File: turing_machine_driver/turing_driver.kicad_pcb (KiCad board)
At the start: 2 copper layers, 165.1 x 110.5 mm, 107 parts, among them J1 Buttons and Switches connector, J2 Header Position Value, J3 Symbol Register Value, J4 State Register Value, J5 External Interface, Q1 55NF06, U1 74LS14, U10 74LS245, U11 SST39SF020, U12 74LS245, U13 74LS245, U14 74LS245, U15 D5631LA, U16 D5631LR, U17 74LS245, U2 74LS03, U3 74LS04, U4 74LS139, U5 74LS74, U6 NE555P, U7 NE555P, U8 NE555P, U9 74LS245

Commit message: added control panel and moved LEDs to it
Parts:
- removed the D1 at (-199.0, 40.3)
- removed D10: LED_HEADER2, LED_THT:LED_D5.0mm
- removed D11: LED_HEADER3, LED_THT:LED_D5.0mm
- removed D12: LED_HEADER4, LED_THT:LED_D5.0mm
- removed D13: LED_HEADER5, LED_THT:LED_D5.0mm
- removed D14: LED_HEADER6, LED_THT:LED_D5.0mm
- removed D15: LED_HEADER7, LED_THT:LED_D5.0mm
- removed D16: LED_HEADER8, LED_THT:LED_D5.0mm
- removed D17: LED_HEADER9, LED_THT:LED_D5.0mm
- removed D18: LED_HEADER10, LED_THT:LED_D5.0mm
- removed D19: LED_HEADER11, LED_THT:LED_D5.0mm
- removed D2: LED_PROGRAM_R, LED_THT:LED_D5.0mm
- removed D20: LED_HEADER12, LED_THT:LED_D5.0mm
- removed D21: LED_HEADER13, LED_THT:LED_D5.0mm
- removed D22: LED_HEADER14, LED_THT:LED_D5.0mm
- removed D23: LED_HEADER15, LED_THT:LED_D5.0mm
- removed D3: LED_RESET_Y, LED_THT:LED_D5.0mm
- removed D4: LED_FINISH_STATE_Y, LED_THT:LED_D5.0mm
- removed D5: LED_SESR_STATE_G, LED_THT:LED_D5.0mm
- removed D6: LED_CLK_G, LED_THT:LED_D5.0mm
- removed D8: LED_HEADER0, LED_THT:LED_D5.0mm
- removed D9: LED_HEADER1, LED_THT:LED_D5.0mm
- removed the R15 at (-151.6, 65.3)
- removed R16, R17, R18, R19, R20, R22, R23, R24, R25, R26, R27, R28, R29, R30, R31, R32, R33, R34, R35, R36, R37: 330Ω, Resistor_THT:R_Axial_DIN0207_L6.3mm_D2.5mm_P10.16mm_Horizontal
- removed the U15 at (-150.4, 39.9)
- removed U16: D5631LR, Display_7Segment:DA56-11CGKWA
- added J6: Signal_connector_1, Connector_Edge:Connector_Edge_2x17pin_odd, F.Cu at (20.3, 129.5)
- added J7: Signal_connector_0, Connector_Edge:Connector_Edge_2x17pin_odd, F.Cu at (20.3, 73.7)
- added REF**: MountingHole_3.2mm_M3, MountingHole:MountingHole_3.2mm_M3, F.Cu at (186.7, 29.2)
- added REF**: MountingHole_3.2mm_M3, MountingHole:MountingHole_3.2mm_M3, F.Cu at (186.7, 132.1)
- added REF**: MountingHole_3.2mm_M3, MountingHole:MountingHole_3.2mm_M3, F.Cu at (29.2, 132.1)
- added REF**: MountingHole_3.2mm_M3, MountingHole:MountingHole_3.2mm_M3, F.Cu at (29.2, 29.2)
- J1: value Buttons and Switches connector -> RPi Interface; footprint Connector_IDC:IDC-Header_2x07_P2.54mm_Horizontal -> Connector_IDC:IDC-Header_2x10_P2.54mm_Vertical
- RN1: value 1,5kΩ -> R_Pack04_SIP; footprint Connector_PinSocket_2.54mm:PinSocket_1x08_P2.54mm_Vertical -> Resistor_THT:R_Array_SIP8
- RN2: value 680Ω -> R_Pack04_SIP; footprint Connector_PinSocket_2.54mm:PinSocket_1x08_P2.54mm_Vertical -> Resistor_THT:R_Array_SIP8
- moved U9 337.7 mm to (124.5, 105.4)
- moved U10 310.3 mm to (106.7, 105.4)
- moved A1 268.5 mm to (161.9, 29.4)
- moved J1 263.8 mm to (176.5, 84.5), turned to -90 degrees
- moved U3 260.7 mm to (177.8, 113.0)
- moved D1 256.5 mm to (64.8, 30.5)
- moved U12 251.5 mm to (71.1, 43.2)
- moved U11 243.0 mm to (55.9, 128.3), turned to 90 degrees
- moved U4 229.4 mm to (160.0, 110.5)
- moved U13 223.7 mm to (35.6, 105.4)
- moved R15 220.7 mm to (61.0, 30.5), turned to 180 degrees
- moved U5 218.8 mm to (142.2, 113.0)
- moved U14 212.5 mm to (53.3, 43.2)
- moved RN1 209.6 mm to (50.5, 110.5), turned to -90 degrees
- moved RN2 201.9 mm to (46.4, 110.5), turned to -90 degrees
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- renumbered C19 to C18, C18 to C19, D7 to D1, R9 to R10, R10 to R12, R21 to R15, R8 to R5, R5 to R6, R6 to R7, R7 to R8, R12 to R9, U17 to U15
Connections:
- A1 pad 13: LPS_{2} -> RRB_{1}
- A1 pad 18: LPS_{2} -> RRB_{1}
- A1 pad 23: LPS_{2} -> RRB_{1}
- A1 pad 28: LPS_{2} -> RRB_{1}
- A1 pad 3: LPS_{2} -> RRB_{1}
- A1 pad 38: LPS_{2} -> RRB_{1}
- A1 pad 8: LPS_{2} -> RRB_{1}
- C1 pad 2: LPS_{2} -> RRB_{1}
- C10 pad 2: LPS_{2} -> RRB_{1}
- C11 pad 2: LPS_{2} -> RRB_{1}
- C12 pad 2: LPS_{2} -> RRB_{1}
- C13 pad 2: LPS_{2} -> RRB_{1}
- C14 pad 2: LPS_{2} -> RRB_{1}
- C15 pad 2: LPS_{2} -> RRB_{1}
- C16 pad 2: LPS_{2} -> RRB_{1}
- C17 pad 2: LPS_{2} -> RRB_{1}
- C18 pad 2: LPS_{2} -> RRB_{1}
- C19 pad 2: LPS_{2} -> RRB_{1}
- C2 pad 2: LPS_{2} -> RRB_{1}
- C20 pad 2: LPS_{2} -> RRB_{1}
- C21 pad 2: LPS_{2} -> RRB_{1}
- C3 pad 2: LPS_{2} -> RRB_{1}
- C4 pad 2: LPS_{2} -> RRB_{1}
- C5 pad 2: LPS_{2} -> RRB_{1}
- C6 pad 2: LPS_{2} -> RRB_{1}
- C7 pad 2: LPS_{2} -> RRB_{1}
- C8 pad 2: LPS_{2} -> RRB_{1}
- C9 pad 2: LPS_{2} -> RRB_{1}
- J1 pad 1: MCB_{0} -> RRB_{1}
- J1 pad 10: LPS_{1} -> ~{DT}
- J1 pad 11: LPS_{2} -> CS_{0}
- J1 pad 12: LBP_{0} -> CS_{1}
- J1 pad 13: LBP_{1} -> D_{6}
- J1 pad 14: LBP_{2} -> D_{7}
- J1 pad 2: MCB_{1} -> LPS_{0}
- J1 pad 3: COM_{0} -> COMBINED_CLK
- J1 pad 4: COM_{1} -> /REPROGRAM
- J1 pad 5: ACP_{0} -> ~{PROGRAM}
- J1 pad 6: ACP_{1} -> ~{FINISH_STATE}
- J1 pad 7: RRB_{0} -> RPI_CLK
- J1 pad 8: LPS_{2} -> ~{RESET}
- J1 pad 9: LPS_{0} -> DDIR
- J5 pad 18: LPS_{2} -> RRB_{1}
- J5 pad 20: LPS_{2} -> RRB_{1}
- J5 pad 22: LPS_{2} -> RRB_{1}
- J5 pad 24: LPS_{2} -> RRB_{1}
- J5 pad 26: LPS_{2} -> RRB_{1}
- J5 pad 28: LPS_{2} -> RRB_{1}
- Q1 pad 3: LPS_{2} -> RRB_{1}
- RN1 pad 2: Net-(RN1-R2.1) -> 7SEG_A
- RN1 pad 3: Net-(RN1-R3.1) -> Net-(RN1-R2.1)
- RN1 pad 4: Net-(RN1-R4.1) -> 7SEG_B
- RN1 pad 5: /LED display/7SEG_D -> Net-(RN1-R3.1)
- RN1 pad 6: /LED display/7SEG_C -> 7SEG_C
- RN1 pad 7: /LED display/7SEG_B -> Net-(RN1-R4.1)
- RN1 pad 8: /LED display/7SEG_A -> 7SEG_D
- RN2 pad 2: Net-(RN2-R2.1) -> 7SEG_E
- RN2 pad 3: Net-(RN2-R3.1) -> Net-(RN2-R2.1)
- RN2 pad 4: Net-(RN2-R4.1) -> 7SEG_F
- RN2 pad 5: /LED display/7SEG_DP -> Net-(RN2-R3.1)
- RN2 pad 6: /LED display/7SEG_G -> 7SEG_G
- RN2 pad 7: /LED display/7SEG_F -> unconnected-(RN2-R4.1-Pad7)
- RN2 pad 8: /LED display/7SEG_E -> unconnected-(RN2-R4.2-Pad8)
- U1 pad 7: LPS_{2} -> RRB_{1}
- U10 pad 10: LPS_{2} -> RRB_{1}
- U10 pad 11: unconnected-(U10-B7-Pad11) -> Net-(U10-B7)
- U10 pad 18: Net-(U10-B0) -> unconnected-(U10-B0-Pad18)
- U10 pad 19: LPS_{2} -> RRB_{1}
- U10 pad 2: SR_{0} -> RRB_{1}
- U10 pad 3: SR_{1} -> SR_{6}
- U10 pad 4: SR_{2} -> SR_{5}
- U10 pad 5: SR_{3} -> SR_{4}
- U10 pad 6: SR_{4} -> SR_{3}
- U10 pad 7: SR_{5} -> SR_{2}
- U10 pad 8: SR_{6} -> SR_{1}
- U10 pad 9: LPS_{2} -> SR_{0}
- U11 pad 1: LPS_{2} -> RRB_{1}
- U11 pad 10: Net-(U11-A2) -> /LED display/QRB_{2}
- U11 pad 11: Net-(U11-A1) -> /LED display/QRB_{1}
- U11 pad 12: Net-(U11-A0) -> /LED display/QRB_{0}
- U11 pad 16: LPS_{2} -> RRB_{1}
- U11 pad 22: LPS_{2} -> RRB_{1}
- U11 pad 23: Net-(U10-B2) -> Net-(U10-B5)
- U11 pad 24: LPS_{2} -> RRB_{1}
- U11 pad 25: Net-(U10-B3) -> Net-(U10-B4)
- U11 pad 26: Net-(U10-B1) -> Net-(U10-B6)
- U11 pad 27: Net-(U10-B0) -> Net-(U10-B7)
- U11 pad 28: Net-(U10-B5) -> Net-(U10-B2)
- U11 pad 29: Net-(U10-B6) -> Net-(U10-B1)
- U11 pad 30: LPS_{2} -> RRB_{1}
- U11 pad 4: Net-(U10-B4) -> Net-(U10-B3)
- U11 pad 5: Net-(U11-A7) -> /LED display/QRB_{7}
- U11 pad 6: Net-(U11-A6) -> /LED display/QRB_{6}
- U11 pad 7: Net-(U11-A5) -> /LED display/QRB_{5}
- U11 pad 8: Net-(U11-A4) -> /LED display/QRB_{4}
- U11 pad 9: Net-(U11-A3) -> /LED display/QRB_{3}
- U12 pad 10: LPS_{2} -> RRB_{1}
- U12 pad 13: Net-(D6-A) -> CLK
- U12 pad 14: Net-(D5-A) -> LED_SESR_STATE
- U12 pad 15: Net-(D4-A) -> LED_FINISH_STATE
- U12 pad 16: Net-(D3-A) -> LED_RESET
- U12 pad 17: Net-(D2-A) -> LED_OPERATE
- U12 pad 18: Net-(D1-A) -> LED_PROGRAM
- U12 pad 8: LPS_{2} -> RRB_{1}
- U12 pad 9: LPS_{2} -> RRB_{1}
- U13 pad 10: LPS_{2} -> RRB_{1}
- U13 pad 11: Net-(RN2-R4.1) -> unconnected-(U13-B7-Pad11)
- U14 pad 1: LPS_{0} -> RRB_{1}
- U14 pad 10: LPS_{2} -> RRB_{1}
- U14 pad 11: Net-(D15-A) -> H_{0}
- U14 pad 12: Net-(D14-A) -> H_{1}
- U14 pad 13: Net-(D13-A) -> H_{2}
- U14 pad 14: Net-(D12-A) -> H_{3}
- U14 pad 15: Net-(D11-A) -> H_{4}
- U14 pad 16: Net-(D10-A) -> H_{5}
- U14 pad 17: Net-(D9-A) -> H_{6}
- U14 pad 18: Net-(D8-A) -> H_{7}
- U14 pad 2: H_{0} -> LED_H_{7}
- U14 pad 3: H_{1} -> LED_H_{6}
- U14 pad 4: H_{2} -> LED_H_{5}
- U14 pad 5: H_{3} -> LED_H_{4}
- U14 pad 6: H_{4} -> LED_H_{3}
- U14 pad 7: H_{5} -> LED_H_{2}
- U14 pad 8: H_{6} -> LED_H_{1}
- U14 pad 9: H_{7} -> LED_H_{0}
- U15 pad 1: LPS_{0} -> RRB_{1}
- U15 pad 10: LPS_{2} -> RRB_{1}
- U15 pad 11: Net-(D23-A) -> H_{8}
- U15 pad 12: Net-(D22-A) -> H_{9}
- U15 pad 13: Net-(D21-A) -> H_{10}
- U15 pad 14: Net-(D20-A) -> H_{11}
- U15 pad 15: Net-(D19-A) -> H_{12}
- U15 pad 16: Net-(D18-A) -> H_{13}
- U15 pad 17: Net-(D17-A) -> H_{14}
- U15 pad 18: Net-(D16-A) -> H_{15}
- U15 pad 2: H_{8} -> LED_H_{15}
- U15 pad 3: H_{9} -> LED_H_{14}
- U15 pad 4: H_{10} -> LED_H_{13}
- U15 pad 5: H_{11} -> LED_H_{12}
- U15 pad 6: H_{12} -> LED_H_{11}
- U15 pad 7: H_{13} -> LED_H_{10}
- U15 pad 8: H_{14} -> LED_H_{9}
- U15 pad 9: H_{15} -> LED_H_{8}
- U2 pad 7: LPS_{2} -> RRB_{1}
- U3 pad 2: Net-(U15-DIG2_CA) -> 7SEG_SYMBOL_0
- U3 pad 4: Net-(U15-DIG1_CA) -> 7SEG_SYMBOL_1
- U3 pad 6: Net-(U16-DIG1_CA) -> 7SEG_STATE_0
- U3 pad 7: LPS_{2} -> RRB_{1}
- U3 pad 8: Net-(U16-DIG2_CA) -> 7SEG_STATE_1
- U4 pad 8: LPS_{2} -> RRB_{1}
- U5 pad 7: LPS_{2} -> RRB_{1}
- U6 pad 1: LPS_{2} -> RRB_{1}
- U7 pad 1: LPS_{2} -> RRB_{1}
- U8 pad 1: LPS_{2} -> RRB_{1}
- U9 pad 10: LPS_{2} -> RRB_{1}
- U9 pad 11: Net-(U11-A7) -> /LED display/QRB_{0}
- U9 pad 12: Net-(U11-A6) -> /LED display/QRB_{1}
- U9 pad 13: Net-(U11-A5) -> /LED display/QRB_{2}
- U9 pad 14: Net-(U11-A4) -> /LED display/QRB_{3}
- U9 pad 15: Net-(U11-A3) -> /LED display/QRB_{4}
- U9 pad 16: Net-(U11-A2) -> /LED display/QRB_{5}
- U9 pad 17: Net-(U11-A1) -> /LED display/QRB_{6}
- U9 pad 18: Net-(U11-A0) -> /LED display/QRB_{7}
- U9 pad 19: LPS_{2} -> RRB_{1}
- U9 pad 2: QR_{0} -> QR_{7}
- U9 pad 3: QR_{1} -> QR_{6}
- U9 pad 4: QR_{2} -> QR_{5}
- U9 pad 5: QR_{3} -> QR_{4}
- U9 pad 6: QR_{4} -> QR_{3}
- U9 pad 7: QR_{5} -> QR_{2}
- U9 pad 8: QR_{6} -> QR_{1}
- U9 pad 9: QR_{7} -> QR_{0}
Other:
- outline, holes or cut-outs redrawn
- board text added: "POWER"
- board text added: "STATE"
- board text added: "SYMBOL"
- board text added: "Signal connector 1"
- board text added: "Signal connector 2"

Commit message: finished driver PCB layout
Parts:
- added C10: 100nF, Capacitor_THT:C_Disc_D3.8mm_W2.6mm_P2.50mm, F.Cu at (116.8, 105.4)
- added C12: 100nF, Capacitor_THT:C_Disc_D3.8mm_W2.6mm_P2.50mm, F.Cu at (78.8, 40.0)
- added C14: 100nF, Capacitor_THT:C_Disc_D3.8mm_W2.6mm_P2.50mm, F.Cu at (61.0, 40.0)
- U6, U7, U8: value NE555P -> 555
- moved C3 275.4 mm to (188.0, 110.5), turned to -90 degrees
- moved R14 258.0 mm to (154.3, 66.0), turned to -90 degrees
- moved C4 257.2 mm to (170.2, 110.5), turned to -90 degrees
- moved R7 255.6 mm to (154.3, 45.1), turned to -90 degrees
- moved R13 252.0 mm to (151.1, 76.2), turned to 90 degrees
- moved R6 250.2 mm to (151.1, 55.2), turned to 90 degrees
- moved C5 239.4 mm to (152.4, 113.0), turned to -90 degrees
- moved R9 232.5 mm to (130.2, 66.7), turned to 180 degrees
- moved R10 232.0 mm to (130.2, 57.1), turned to 180 degrees
- moved C7 229.7 mm to (150.5, 42.5)
- moved C8 228.9 mm to (150.5, 63.5)
- moved C19 224.2 mm to (148.0, 55.2), turned to 180 degrees
- moved R11 222.4 mm to (120.0, 63.5)
- moved R12 222.2 mm to (120.0, 60.3)
- moved C24 222.2 mm to (148.0, 76.2), turned to 180 degrees
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- renumbered C10 to C11, C11 to C13, C12 to C15, C13 to C16, C14 to C17, C15 to C18, C16 to C19, C17 to C20, C18 to C21, C19 to C22, C20 to C23, C21 to C24
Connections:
- C17 pad 1: Net-(C14-Pad1) -> (no net)
- C21 pad 1: Net-(C18-Pad1) -> (no net)
- C22 pad 1: Net-(C19-Pad1) -> (no net)
- R1 pad 1: Net-(C14-Pad1) -> Net-(C17-Pad1)
- R10 pad 2: Net-(C19-Pad1) -> Net-(C22-Pad1)
- R11 pad 1: Net-(C18-Pad1) -> Net-(C21-Pad1)
- R12 pad 1: Net-(C19-Pad1) -> Net-(C22-Pad1)
- R2 pad 2: Net-(C14-Pad1) -> Net-(C17-Pad1)
- R9 pad 2: Net-(C18-Pad1) -> Net-(C21-Pad1)
- U1 pad 1: Net-(C19-Pad1) -> Net-(C22-Pad1)
- U1 pad 3: Net-(C18-Pad1) -> Net-(C21-Pad1)
- U1 pad 5: Net-(C14-Pad1) -> Net-(C17-Pad1)
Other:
- board text added: "HEADER"

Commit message: added some wiring and fixed few schematic bugs
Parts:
- U6, U7, U8: value 555 -> NE555P
- moved C11 5.08 mm to (61.0, 110.5)
- moved U11 5.08 mm to (61.0, 128.3)
- moved RN1 3.45 mm to (54.0, 110.5)
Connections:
- C17 pad 1: (no net) -> Net-(C17-Pad1)
- C21 pad 1: (no net) -> Net-(C21-Pad1)
- C22 pad 1: (no net) -> Net-(C22-Pad1)
- R15 pad 2: LED_GND -> RRB_{1}
- U4 pad 13: unconnected-(U4B-A1-Pad13) -> LPS_{0}
- U4 pad 14: unconnected-(U4B-A0-Pad14) -> LPS_{0}
- U4 pad 15: unconnected-(U4B-E-Pad15) -> LPS_{0}
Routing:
- net RRB_{1}: track 0.00 -> 949.8 mm, vias 0 -> 23
- net LPS_{0}: track 0.00 -> 699.9 mm, vias 0 -> 13
- net LPS_{1}: track 0.00 -> 255.4 mm, vias 0 -> 4
- net CLK: track 0.00 -> 201.2 mm, vias 0 -> 6
- net ~{PROGRAM}: track 0.00 -> 177.1 mm, vias 0 -> 5
- net Net-(U11-A16): track 0.00 -> 173.6 mm, vias 0 -> 7
- net SESR_STATE: track 0.00 -> 169.3 mm, vias 0 -> 3
- net Net-(U11-A15): track 0.00 -> 164.6 mm, vias 0 -> 7
- net COMBINED_CLK: track 0.00 -> 158.7 mm, vias 0 -> 7
- net /REPROGRAM: track 0.00 -> 148.4 mm, vias 0 -> 6
- net D_{0}: track 0.00 -> 124.5 mm, vias 0 -> 3
- net D_{1}: track 0.00 -> 124.1 mm, vias 0 -> 4
- net RPI_CLK: track 0.00 -> 118.5 mm, vias 0 -> 3
- net /LED display/QRB_{7}: track 0.00 -> 109.0 mm, vias 0 -> 5
- net D_{2}: track 0.00 -> 108.5 mm, vias 0 -> 3
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
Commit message: finished driver PCB wiring and added some marks
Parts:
- added REF**: KiCad-Logo2_8mm_SilkScreen, Symbol:KiCad-Logo2_8mm_SilkScreen, B.Cu at (93.3, 88.9)
- added REF**: OSHW-Logo_11.4x12mm_SilkScreen, Symbol:OSHW-Logo_11.4x12mm_SilkScreen, B.Cu at (120.7, 90.8)
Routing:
- net 7SEG_STATE_1: track 0.00 -> 207.7 mm, vias 0 -> 5
- net 7SEG_STATE_0: track 0.00 -> 199.3 mm, vias 0 -> 7
- net 7SEG_SYMBOL_1: track 0.00 -> 194.6 mm, vias 0 -> 6
- net 7SEG_SYMBOL_0: track 0.00 -> 191.2 mm, vias 0 -> 7
- net ACP_{0}: track 0.00 -> 179.8 mm, vias 0 -> 4
- net /LED display/RESET: track 0.00 -> 173.6 mm, vias 0 -> 5
- net /LED display/FINISH_STATE: track 0.00 -> 166.4 mm, vias 0 -> 5
- net MCB_{0}: track 0.00 -> 164.1 mm, vias 0 -> 3
- net ACP_{1}: track 21.0 -> 183.2 mm, vias 0 -> 4
- net RRB_{0}: track 0.00 -> 157.2 mm, vias 0 -> 3
- net COM_{0}: track 0.00 -> 153.1 mm, vias 0 -> 3
- net LBP_{1}: track 0.00 -> 144.3 mm, vias 0 -> 3
- net LBP_{2}: track 0.00 -> 126.0 mm, vias 0 -> 3
- net ~{LED_PWR_CLK}: track 40.5 -> 166.4 mm, vias 2 -> 4
- net /Clock and Interfaces/AUTO_CLK: track 0.00 -> 59.0 mm, vias 0 -> 1
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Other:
- outline, holes or cut-outs redrawn
- board text added: "Paweł Szymański 02.2026"
- board text added: "Sterownik Urządzenia"
- board text added: "Tura"

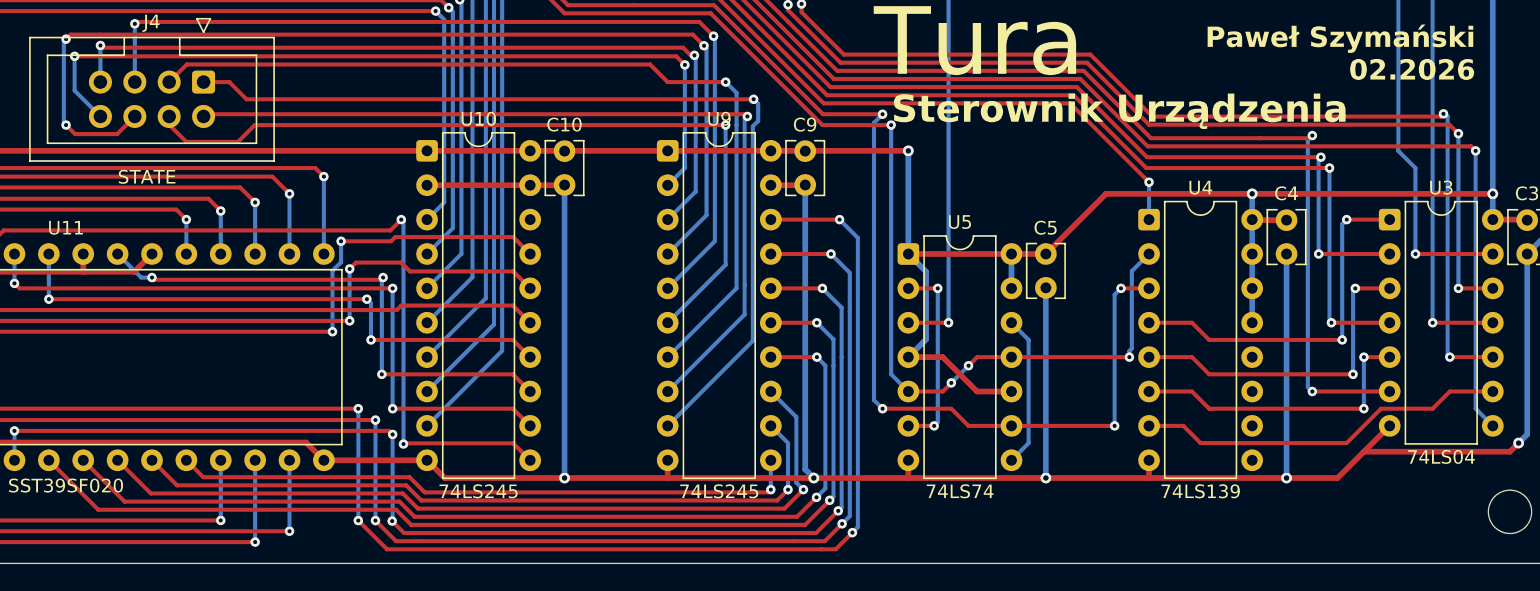
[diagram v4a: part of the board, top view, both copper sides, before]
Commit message: added few markings to PCBs
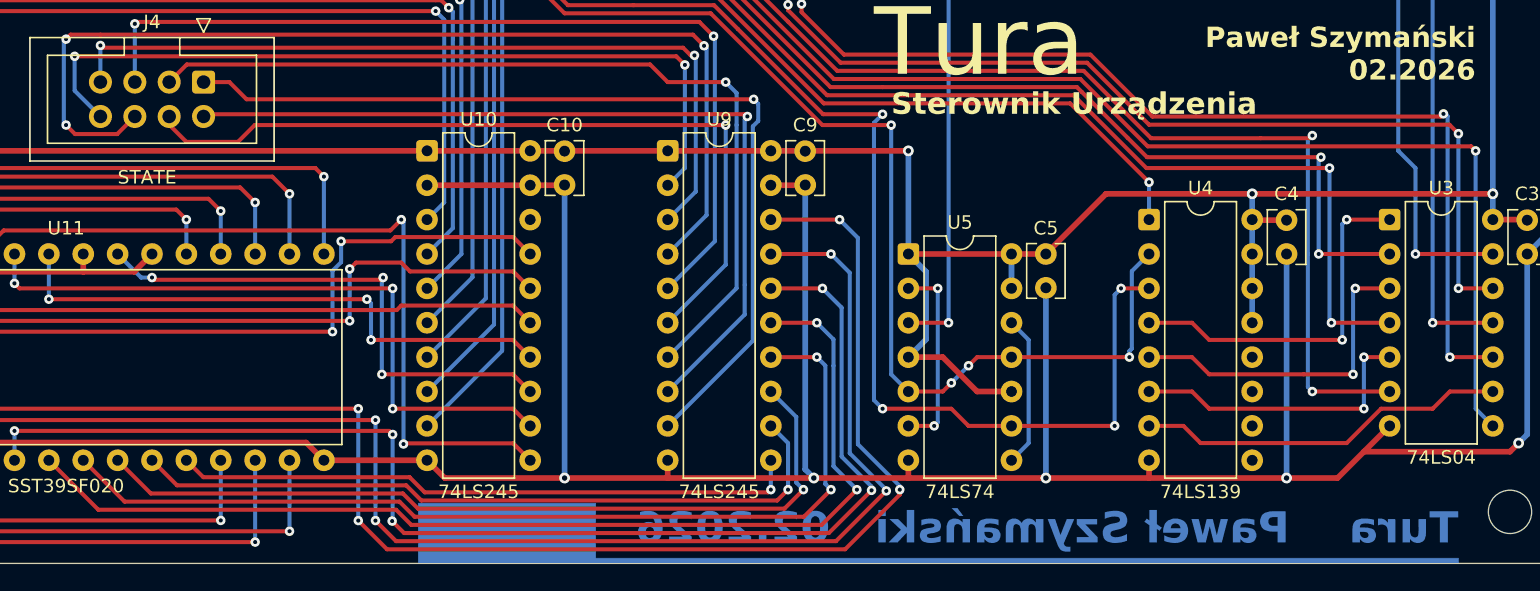
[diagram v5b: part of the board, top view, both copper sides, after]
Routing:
- net /LED display/QRB_{7}: track 109.0 -> 112.0 mm
- net /LED display/QRB_{6}: track 100.2 -> 102.9 mm
- net /LED display/QRB_{5}: track 91.6 -> 94.0 mm
- net /LED display/QRB_{4}: track 77.6 -> 79.7 mm
- net /LED display/QRB_{3}: track 70.8 -> 71.4 mm
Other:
- board text added: "Tura Paweł Szymański 02.2026"
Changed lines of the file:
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@@
 		(net 159)
 	)
+	(gr_rect
+		(start 106.045 131.445)
+		(end 119.126 135.89)
+		(stroke
+			(width 0.05)
+			(type solid)
+		)
+		(fill yes)
+		(layer "B.Cu")
+	)
+	(gr_rect
+		(start 119.126 135.509)
+		(end 182.88 135.89)
+		(stroke
+			(width 0.05)
+			(type solid)
+		)
+		(fill yes)
+		(layer "B.Cu")
+	)
 	(gr_poly
 		(pts
@@
 		(layer "Edge.Cuts")
 	)
+	(gr_text "Tura    Paweł Szymański   02.2026"
+		(at 182.88 134.62 0)
+		(layer "B.Cu" knockout)
+		(effects
+			(font
+				(size 2.3 2.3)
+				(thickness 0.46)
+				(bold yes)
+			)
+			(justify left bottom mirror)
+		)
+	)
 	(gr_text "Paweł Szymański\n02.2026"
 		(at 184.15 100.33 0)
@@
 	)
 	(gr_text "Sterownik Urządzenia"
-		(at 140.97 103.505 0)
+		(at 140.97 102.87 0)
 		(layer "F.SilkS")
 		(effects
 			(font
-				(size 2 2)
-				(thickness 0.33)
+				(size 1.6 1.6)
+				(thickness 0.32)
 				(bold yes)
 			)
@@
 	)
 	(segment
+		(start 138.437096 130.440999)
+		(end 135.833095 133.045)
+		(width 0.3)
+		(layer "F.Cu")
+		(net 133)
+	)
+	(segment
 		(start 82.395 131.925)
 		(end 78.74 128.27)
@@
 	)
 	(segment
-		(start 136.428974 131.230811)
+		(start 135.833095 133.045)
 		(end 134.614785 133.045)
 		(width 0.3)
@@
 	)
 	(via
-		(at 136.428974 131.230811)
+		(at 138.437096 130.440999)
 		(size 0.7)
 		(drill 0.3)
@@
 	)
 	(segment
-		(start 136.707 130.952785)
-		(end 136.428974 131.230811)
+		(start 136.707 128.710903)
+		(end 138.437096 130.440999)
 		(width 0.3)
 		(layer "B.Cu")
@@
 	)
 	(segment
-		(start 136.707 121.285)
-		(end 136.707 130.952785)
+		(start 135.48 118.11)
+		(end 136.707 119.337)
 		(width 0.3)
 		(layer "B.Cu")
@@
 	)
 	(segment
-		(start 135.48 118.11)
-		(end 136.707 119.337)
+		(start 136.707 121.285)
+		(end 136.707 128.710903)
 		(width 0.3)
 		(layer "B.Cu")
@@
 	)
 	(segment
-		(start 135.816937 134.848)
+		(start 137.567 134.848)
 		(end 103.723 134.848)
 		(width 0.3)
@@
 	)
 	(segment
-		(start 138.105551 133.617672)
-		(end 136.875223 134.848)
+		(start 141.605 130.441)
+		(end 141.605 130.81)
 		(width 0.3)
 		(layer "F.Cu")
@@
 	)
 	(segment
-		(start 136.875223 134.848)
-		(end 135.816937 134.848)
+		(start 132.08 110.49)
+		(end 137.16 110.49)
 		(width 0.3)
 		(layer "F.Cu")
@@
 	)
 	(segment
-		(start 132.08 110.49)
-		(end 137.16 110.49)
+		(start 141.605 130.81)
+		(end 137.567 134.848)
 		(width 0.3)
 		(layer "F.Cu")
@@
 	)
 	(via
-		(at 138.105551 133.617672)
+		(at 141.605 130.441)
 		(size 0.7)
 		(drill 0.3)
@@
 	)
 	(segment
-		(start 138.51 111.84)
-		(end 138.51 115.57)
-		(width 0.3)
-		(layer "B.Cu")
-		(net 134)
-	)
-	(segment
 		(start 71.12 125.095)
 		(end 71.12 128.27)
@@
 	)
 	(segment
-		(start 138.51 130.175)
-		(end 138.51 133.213223)
+		(start 101.6 132.725)
+		(end 101.6 124.46)
 		(width 0.3)
 		(layer "B.Cu")
@@
 	)
 	(segment
-		(start 101.6 132.725)
-		(end 101.6 124.46)
+		(start 138.51 127.08)
+		(end 138.51 111.84)
 		(width 0.3)
 		(layer "B.Cu")
@@
 	)
 	(segment
-		(start 137.16 110.49)
-		(end 138.51 111.84)
+		(start 141.605 130.441)
+		(end 141.605 130.175)
 		(width 0.3)
 		(layer "B.Cu")
@@
 	)
 	(segment
-		(start 138.51 115.57)
-		(end 138.51 130.175)
+		(start 141.605 130.175)
+		(end 138.51 127.08)
 		(width 0.3)
 		(layer "B.Cu")
@@
 	)
 	(segment
-		(start 138.51 133.213223)
-		(end 138.105551 133.617672)
+		(start 138.51 111.84)
+		(end 137.16 110.49)
 		(width 0.3)
 		(layer "B.Cu")
@@
 	(segment
 		(start 105.764174 132.444)
-		(end 104.644174 131.324)
+		(end 134.522 132.444)
 		(width 0.3)
 		(layer "F.Cu")
@@
 	(segment
 		(start 104.644174 131.324)
-		(end 84.334 131.324)
+		(end 105.764174 132.444)
 		(width 0.3)
 		(layer "F.Cu")
@@
 	)
 	(segment
-		(start 134.018806 132.444)
-		(end 105.764174 132.444)
+		(start 81.28 128.27)
+		(end 84.334 131.324)
 		(width 0.3)
 		(layer "F.Cu")
@@
 	(segment
 		(start 84.334 131.324)
-		(end 81.28 128.27)
+		(end 104.644174 131.324)
 		(width 0.3)
 		(layer "F.Cu")
@@
 	)
 	(segment
-		(start 135.453903 131.008903)
-		(end 134.018806 132.444)
+		(start 134.522 132.444)
+		(end 136.525 130.441)
 		(width 0.3)
 		(layer "F.Cu")
@@
 	)
 	(via
-		(at 135.453903 131.008903)
+		(at 136.525 130.441)
 		(size 0.7)
 		(drill 0.3)
@@
 	)
 	(segment
-		(start 136.106 130.356806)
+		(start 136.106 130.022)
 		(end 136.106 121.276)
 		(width 0.3)
@@
 	)
 	(segment
-		(start 135.453903 131.008903)
-		(end 136.106 130.356806)
+		(start 136.525 130.441)
+		(end 136.106 130.022)
 		(width 0.3)
 		(layer "B.Cu")
@@
 	)
 	(segment
-		(start 137.058806 132.007546)
-		(end 135.420352 133.646)
-		(width 0.3)
-		(layer "F.Cu")
-		(net 138)
-	)
-	(segment
-		(start 134.013785 133.646)
+		(start 136.363466 133.646)
 		(end 104.98486 133.646)
 		(width 0.3)
@@
 	)
 	(segment
-		(start 135.420352 133.646)
-		(end 134.013785 133.646)
+		(start 139.519047 130.490419)
+		(end 136.363466 133.646)
 		(width 0.3)
 		(layer "F.Cu")
@@
 	)
 	(via
-		(at 137.058806 132.007546)
+		(at 139.519047 130.490419)
 		(size 0.7)
 		(drill 0.3)
@@
 	)
 	(segment
-		(start 137.308 116.988)
-		(end 137.308 120.65)
+		(start 137.308 127.997942)
+		(end 137.308 116.988)
 		(width 0.3)
 		(layer "B.Cu")
@@
 	)
 	(segment
-		(start 104.10193 132.76307)
-		(end 104.14 132.725)
+		(start 139.519047 130.208989)
+		(end 137.308 127.997942)
 		(width 0.3)
 		(layer "B.Cu")
@@
 	)
 	(segment
-		(start 104.14 132.725)
-		(end 104.14 126.365)
+		(start 104.10193 132.76307)
+		(end 104.14 132.725)
 		(width 0.3)
 		(layer "B.Cu")
@@
 	)
 	(segment
-		(start 76.2 126.099)
-		(end 76.2 128.27)
+		(start 104.14 132.725)
+		(end 104.14 126.365)
 		(width 0.3)
 		(layer "B.Cu")
@@
 	)
 	(segment
-		(start 135.89 115.57)
-		(end 137.308 116.988)
+		(start 139.519047 130.490419)
+		(end 139.519047 130.208989)
 		(width 0.3)
 		(layer "B.Cu")
@@
 	)
 	(segment
-		(start 137.308 131.758352)
-		(end 137.058806 132.007546)
+		(start 76.2 126.099)
+		(end 76.2 128.27)
 		(width 0.3)
 		(layer "B.Cu")
@@
 	)
 	(segment
-		(start 137.308 120.65)
-		(end 137.308 131.758352)
+		(start 137.308 116.988)
+		(end 135.89 115.57)
 		(width 0.3)
 		(layer "B.Cu")
@@
 	)
 	(segment
-		(start 106.045 134.247)
+		(start 136.893838 134.247)
 		(end 104.392 134.247)
 		(width 0.3)
@@
 	)
 	(segment
-		(start 137.348086 132.964793)
-		(end 136.065879 134.247)
-		(width 0.3)
-		(layer "F.Cu")
-		(net 139)
-	)
-	(segment
-		(start 104.392 134.247)
-		(end 102.87 132.725)
-		(width 0.3)
-		(layer "F.Cu")
-		(net 139)
-	)
-	(segment
-		(start 133.764843 134.247)
-		(end 106.045 134.247)
+		(start 140.60912 130.531718)
+		(end 136.893838 134.247)
 		(width 0.3)
 		(layer "F.Cu")
@@
 	)
 	(segment
-		(start 132.08 113.03)
-		(end 136.525 113.03)
+		(start 104.392 134.247)
+		(end 102.87 132.725)
 		(width 0.3)
 		(layer "F.Cu")
@@
 	)
 	(segment
-		(start 136.065879 134.247)
-		(end 133.764843 134.247)
+		(start 132.08 113.03)
+		(end 136.525 113.03)
 		(width 0.3)
 		(layer "F.Cu")
@@
 	)
 	(via
-		(at 137.348086 132.964793)
+		(at 140.60912 130.531718)
 		(size 0.7)
 		(drill 0.3)
@@
 	)
 	(segment
-		(start 137.909 117.236942)
-		(end 137.909 132.403879)
+		(start 137.909 127.749)
+		(end 137.909 114.414)
 		(width 0.3)
 		(layer "B.Cu")
@@
 	)
 	(segment
-		(start 102.87 132.725)
-		(end 102.87 125.299)
+		(start 140.60912 130.44912)
+		(end 137.909 127.749)
 		(width 0.3)
 		(layer "B.Cu")
@@
 	)
 	(segment
-		(start 137.909 132.403879)
-		(end 137.348086 132.964793)
+		(start 140.60912 130.531718)
+		(end 140.60912 130.44912)
 		(width 0.3)
 		(layer "B.Cu")
@@
 	)
 	(segment
-		(start 73.66 125.73)
-		(end 73.66 128.27)
+		(start 102.87 132.725)
+		(end 102.87 125.299)
 		(width 0.3)
 		(layer "B.Cu")
@@
 	)
 	(segment
-		(start 137.909 114.414)
-		(end 137.909 117.236942)
+		(start 73.66 125.73)
+		(end 73.66 128.27)
 		(width 0.3)
 		(layer "B.Cu")
@@
 	)
 	(segment
-		(start 136.525 113.03)
-		(end 137.909 114.414)
+		(start 137.909 114.414)
+		(end 136.525 113.03)
 		(width 0.3)
 		(layer "B.Cu")
